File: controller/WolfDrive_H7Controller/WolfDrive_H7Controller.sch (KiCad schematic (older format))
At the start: 320 parts, among them CN10 CONN_02X17, CN7 CONN_02X10, CN8 CONN_02X08, CN9 CONN_02X15, CON1 SD_Card, J1 USB_OTG, J10 GND, J11 GND, J12 12VA, J13 Regen, J14 Throttle, J15 PWM1, J16 PWM2, J17 PWM3, J18 ~PWM1, J19 ~PWM2, J2 QSPI_CLK, J20 ~PWM3, J21 OCV, J22 ~F_C, J23 ~F_B, J24 ~F_A, J25 Overtemp, J26 PWM_EN, J27 Conn_01x04_Female, J28 GS3, J29 Conn_01x04, J3 QSPI_NCS, J30 SPI2_SCK, J31 SPI2_NSS, J32 SPI2_MOSI, J33 SPI2_MISO, J34 PS-DIS, J35 3V3, J36 GND, J37 GND, J38 AGND, J39 SP1_MISO, J4 QSPI_IO0, J40 SP1_SCK, J41 SP1_NSS, J42 SP1_MOSI, J43 GS3, J44 GS3, J45 GS3, J46 GS3, J47 GS3, J48 GS3, J49 GS3, J5 QSPI_IO1, J50 GS3, J51 GS3, J52 GS3, J53 GS3, J54 GS3, J55 GS3, J56 GS3, J6 QSPI_IO2, J7 QSPI_IO3, J8 12V, J9 GND, P1 GATE_IO_A, P10 GATE_IO_A, P11 GATE_IO_A, P7 CONN_01X02, P9 GATE_IO_A, U1 LM1117-5.0, U10 74HC266, U11 FT232RL, U12 74LVC1G02, U13 74LVC1G02, U14 74LVC1G02, U15 74LVC1G02, U16 74LVC1G02, U17 74LVC1G02, U18 74LVC1G02, U19 74LVC1G02, U2 LM1117-3.3, U20 74HC266, U21 74LVC1G02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

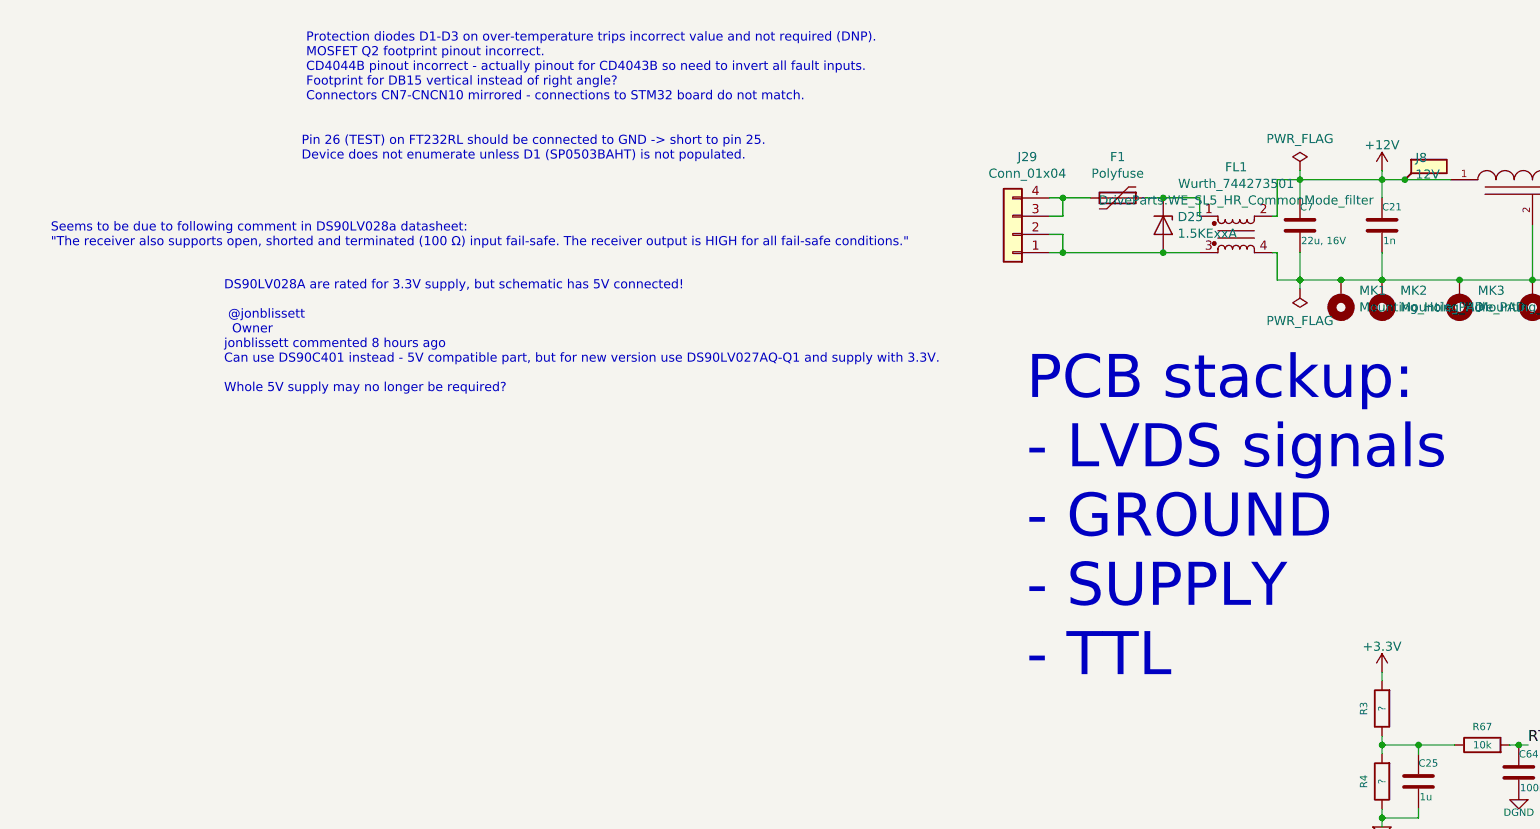
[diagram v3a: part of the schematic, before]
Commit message: Amended input protection
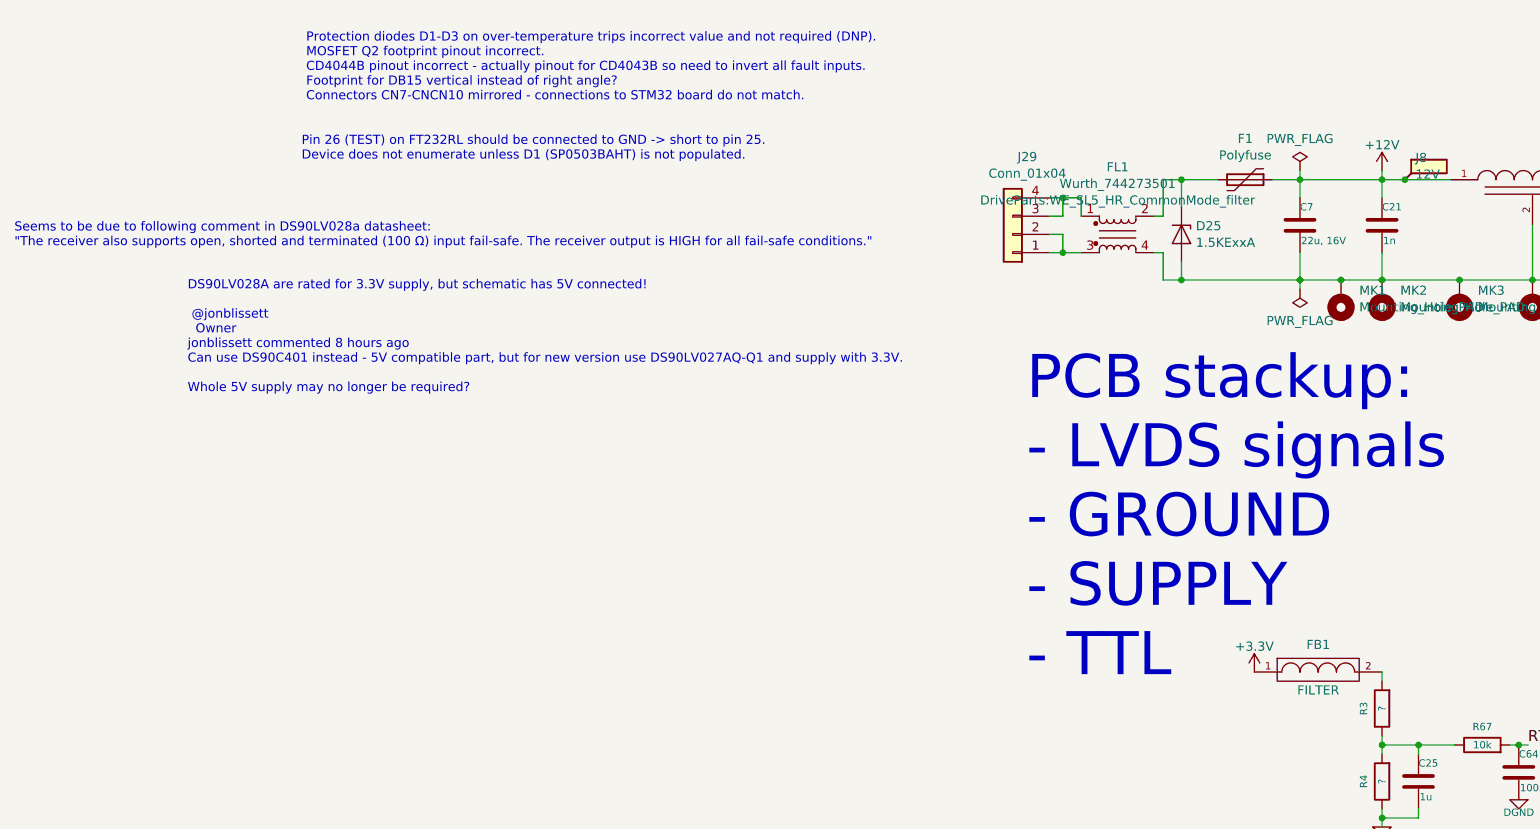
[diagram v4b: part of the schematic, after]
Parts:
- added FB1: FILTER, w_smd_inductors:inductor_smd_0805, symbol WolfDrive_H7Controller-rescue:WolfDrive_H7Controller-rescue_FILTER-RESCUE-WolfD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
- F1: footprint (none) -> Fuse:Fuse_1812_4532Metric_Pad1.24x3.50mm_HandSolder
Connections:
- net +12V: now also F1.1; no longer FL1.2
- net +3V3: now also FB1.1; no longer R3.2
- net DGND: now also D25.2 (A2)
- net at FL1.3, J29.1 (Pin_1), J29.2 (Pin_2): no longer D25.2 (A2)
- net at J29.3 (Pin_3), J29.4 (Pin_4): now also FL1.1; no longer F1.2
- new net: FB1.2, R3.2
- new net: D25.1 (A1), F1.2, FL1.2
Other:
- moved on the sheet: D25, FL1
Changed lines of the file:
@@
 Connection ~ 2450 1550
 Wire Wire Line
-	2325 1550 2450 1550
-Wire Wire Line
 	1075 1850 1150 1850
 Wire Wire Line
@@
 	4275 2000 4275 2100
 Wire Wire Line
-	2325 2100 2450 2100
-Wire Wire Line
 	6150 2625 6350 2625
 Wire Wire Line
@@
 	-1   0    0    1
 $EndComp
-Wire Wire Line
-	1075 1950 1150 1950
-Wire Wire Line
-	1150 1850 1150 1950
 Text Notes 21575 2400 0    50   ~ 0
 SHB11-PBPC-D08-ST-BK
@@
 L Device:EMI_Filter_CommonMode FL1
 U 1 1 5AE9439E
-P 2100 1850
-F 0 "FL1" H 2100 2219 50  0000 C CNN
-F 1 "Wurth_744273501" H 2100 2128 50  0000 C CNN
-F 2 "DriveParts:WE_SL5_HR_CommonMode_filter" H 2100 2037 50  0000 C CNN
-F 3 "~" V 2100 1890 50  0000 C CNN
-	1    2100 1850
+P 1450 1850
+F 0 "FL1" H 1450 2219 50  0000 C CNN
+F 1 "Wurth_744273501" H 1450 2128 50  0000 C CNN
+F 2 "DriveParts:WE_SL5_HR_CommonMode_filter" H 1450 2037 50  0000 C CNN
+F 3 "~" V 1450 1890 50  0000 C CNN
+	1    1450 1850
 	1    0    0    -1
 $EndComp
-Wire Wire Line
-	2325 1550 2325 1750
-Wire Wire Line
-	2325 1750 2300 1750
-Wire Wire Line
-	2300 1950 2325 1950
-Wire Wire Line
-	2325 1950 2325 2100
 Connection ~ 2450 2100
-Connection ~ 1150 1950
 Wire Wire Line
 	1075 1750 1150 1750
@@
 Wire Wire Line
 	9950 4800 10550 4800
-Text Notes -3000 1125 0    50   ~ 0
-Protection diodes D1-D3 on over-temperature trips incorrect value and not required (DNP).\nMOSFET Q2 footprint pinout incorrect.\nCD4044B pinout incorrect - actually pinout for CD4043B so need to invert all fault inputs.\nFootprint for DB15 vertical instead of right angle?\nConnectors CN7-CNCN10 mirrored - connections to STM32 board do not match.
-Text Notes -3025 1450 0    50   ~ 0
-Pin 26 (TEST) on FT232RL should be connected to GND -> short to pin 25.\nDevice does not enumerate unless D1 (SP0503BAHT) is not populated.
-Text Notes -4400 1925 0    50   ~ 0
-Seems to be due to following comment in DS90LV028a datasheet:\n"The receiver also supports open, shorted and terminated (100 Ω) input fail-safe. The receiver output is HIGH for all fail-safe conditions."
-Text Notes -3450 2725 0    50   ~ 0
-DS90LV028A are rated for 3.3V supply, but schematic has 5V connected!\n\n @jonblissett\n  Owner\njonblissett commented 8 hours ago\nCan use DS90C401 instead - 5V compatible part, but for new version use DS90LV027AQ-Q1 and supply with 3.3V.\n\nWhole 5V supply may no longer be required?
 $Comp
 L WolfDrive_H7Controller-rescue:power_+3.3V-RESCUE-WolfDrive_H7Controller-WolfDrive_H7Controller-rescue #PWR0107
@@
 Wire Wire Line
 	21350 12250 21500 12250
-$Comp
-L WolfDrive_H7Controller-rescue:power_+3.3V-RESCUE-WolfDrive_H7Controller-WolfDrive_H7Controller-rescue #PWR0191
-U 1 1 61BC542C
-P 2900 4250
-F 0 "#PWR0191" H 2900 4100 50  0001 C CNN
-F 1 "+3.3V" H 2900 4390 50  0000 C CNN
-F 2 "" H 2900 4250 60  0000 C CNN
-F 3 "" H 2900 4250 60  0000 C CNN
-	1    2900 4250
-	1    0    0    -1
-$EndComp
 Connection ~ 6750 2625
 Wire Wire Line
@@
 	1    0    0    -1
 $EndComp
+Text Notes -3025 1450 0    50   ~ 0
+Pin 26 (TEST) on FT232RL should be connected to GND -> short to pin 25.\nDevice does not enumerate unless D1 (SP0503BAHT) is not populated.
+Text Notes -4600 1925 0    50   ~ 0
+Seems to be due to following comment in DS90LV028a datasheet:\n"The receiver also supports open, shorted and terminated (100 Ω) input fail-safe. The receiver output is HIGH for all fail-safe conditions."
+Text Notes -3000 1125 0    50   ~ 0
+Protection diodes D1-D3 on over-temperature trips incorrect value and not required (DNP).\nMOSFET Q2 footprint pinout incorrect.\nCD4044B pinout incorrect - actually pinout for CD4043B so need to invert all fault inputs.\nFootprint for DB15 vertical instead of right angle?\nConnectors CN7-CNCN10 mirrored - connections to STM32 board do not match.
+Text Notes -3650 2725 0    50   ~ 0
+DS90LV028A are rated for 3.3V supply, but schematic has 5V connected!\n\n @jonblissett\n  Owner\njonblissett commented 8 hours ago\nCan use DS90C401 instead - 5V compatible part, but for new version use DS90LV027AQ-Q1 and supply with 3.3V.\n\nWhole 5V supply may no longer be required?
+Wire Wire Line
+	1150 1850 1150 1950
+Connection ~ 1150 1950
 Wire Wire Line
-	1900 1750 1900 1650
+	1075 1950 1150 1950
+Wire Wire Line
+	1250 1750 1250 1650
+Connection ~ 1150 1650
 $Comp
 L Diode:1.5KExxA D25
 U 1 1 5B0319FA
-P 1700 1800
-F 0 "D25" V 1654 1879 50  0000 L CNN
-F 1 "1.5KExxA" V 1745 1879 50  0000 L CNN
-F 2 "Diode_SMD:D_SMB-SMC_Universal_Handsoldering" H 1700 1600 50  0001 C CNN
-F 3 "https://www.vishay.com/docs/88301/15ke.pdf" H 1650 1800 50  0001 C CNN
-	1    1700 1800
+P 1800 1850
+F 0 "D25" V 1754 1929 50  0000 L CNN
+F 1 "1.5KExxA" V 1845 1929 50  0000 L CNN
+F 2 "Diode_SMD:D_SMB-SMC_Universal_Handsoldering" H 1800 1650 50  0001 C CNN
+F 3 "https://www.vishay.com/docs/88301/15ke.pdf" H 1750 1850 50  0001 C CNN
+	1    1800 1850
 	0    1    1    0
 $EndComp
 Wire Wire Line
-	1150 1950 1700 1950
+	1150 1950 1250 1950
 Wire Wire Line
-	1700 1650 1900 1650
-Connection ~ 1700 1950
-Wire Wire Line
-	1700 1950 1900 1950
+	1150 1650 1250 1650
 $Comp
 L Device:Polyfuse F1
-U 1 1 5B3954F5
-P 1450 1650
-F 0 "F1" V 1225 1650 50  0000 C CNN
-F 1 "Polyfuse" V 1316 1650 50  0000 C CNN
-F 2 "" H 1500 1450 50  0001 L CNN
-F 3 "~" H 1450 1650 50  0001 C CNN
-	1    1450 1650
+U 1 1 5D0A55F3
+P 2150 1550
+F 0 "F1" V 1925 1550 50  0000 C CNN
+F 1 "Polyfuse" V 2016 1550 50  0000 C CNN
+F 2 "Fuse:Fuse_1812_4532Metric_Pad1.24x3.50mm_HandSolder" H 2200 1350 50  0001 L CNN
+F 3 "~" H 2150 1550 50  0001 C CNN
+	1    2150 1550
 	0    1    1    0
 $EndComp
 Wire Wire Line
-	1300 1650 1150 1650
-Connection ~ 1150 1650
+	2300 1550 2450 1550
+Wire Wire Line
+	2000 1550 1800 1550
+Wire Wire Line
+	1800 1550 1800 1700
+Wire Wire Line
+	1650 1750 1700 1750
+Wire Wire Line
+	1700 1750 1700 1550
 Wire Wire Line
-	1600 1650 1700 1650
-Connection ~ 1700 1650
+	1700 1550 1800 1550
+Connection ~ 1800 1550
+Wire Wire Line
+	1650 1950 1700 1950
+Wire Wire Line
+	1700 1950 1700 2100
+Wire Wire Line
+	1700 2100 1800 2100
+Wire Wire Line
+	1800 2000 1800 2100
+Connection ~ 1800 2100
+Wire Wire Line
+	1800 2100 2450 2100
+$Comp
+L WolfDrive_H7Controller-rescue:power_+3.3V-RESCUE-WolfDrive_H7Controller-WolfDrive_H7Controller-rescue #PWR0191
+U 1 1 61BC542C
+P 2200 4250
+F 0 "#PWR0191" H 2200 4100 50  0001 C CNN
+F 1 "+3.3V" H 2200 4390 50  0000 C CNN
+F 2 "" H 2200 4250 60  0000 C CNN
+F 3 "" H 2200 4250 60  0000 C CNN
+	1    2200 4250
+	1    0    0    -1
+$EndComp
+$Comp
+L WolfDrive_H7Controller-rescue:WolfDrive_H7Controller-rescue_FILTER-RESCUE-WolfDrive_H7Controller-WolfDrive_H7Controller-rescue FB1
+U 1 1 5D76AC8F
+P 2550 4250
+F 0 "FB1" H 2550 4400 50  0000 C CNN
+F 1 "FILTER" H 2550 4150 50  0000 C CNN
+F 2 "w_smd_inductors:inductor_smd_0805" H 2550 4250 50  0001 C CNN
+F 3 "" H 2550 4250 50  0000 C CNN
+	1    2550 4250
+	1    0    0    -1
+$EndComp
 $EndSCHEMATC

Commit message: updated footprints
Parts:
- P1, P10, P11, P9: footprint Connectors:IDC_Header_Straight_16pins -> Connectors_IDC:IDC-Header_2x08_Pitch2.54mm_Straight
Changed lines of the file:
@@
 F 0 "P10" H 21625 4225 50  0000 C CNN
 F 1 "GATE_IO_A" V 21625 3775 50  0000 C CNN
-F 2 "Connectors:IDC_Header_Straight_16pins" H 21625 2575 50  0001 C CNN
+F 2 "Connectors_IDC:IDC-Header_2x08_Pitch2.54mm_Straight" H 21625 2575 50  0001 C CNN
 F 3 "" H 21625 2575 50  0000 C CNN
 	1    21625 3775
@@
 F 0 "P11" H 21625 6325 50  0000 C CNN
 F 1 "GATE_IO_A" V 21625 5875 50  0000 C CNN
-F 2 "Connectors:IDC_Header_Straight_16pins" H 21625 4675 50  0001 C CNN
+F 2 "Connectors_IDC:IDC-Header_2x08_Pitch2.54mm_Straight" H 21625 4675 50  0001 C CNN
 F 3 "" H 21625 4675 50  0000 C CNN
 	1    21625 5875
@@
 F 0 "P9" H 21625 2275 50  0000 C CNN
 F 1 "GATE_IO_A" V 21625 1825 50  0000 C CNN
-F 2 "Connectors:IDC_Header_Straight_16pins" H 21625 625 50  0001 C CNN
+F 2 "Connectors_IDC:IDC-Header_2x08_Pitch2.54mm_Straight" H 21625 625 50  0001 C CNN
 F 3 "" H 21625 625 50  0000 C CNN
 	1    21625 1825
@@
 F 0 "P1" H 9900 10950 50  0000 C CNN
 F 1 "GATE_IO_A" V 9900 10500 50  0000 C CNN
-F 2 "Connectors:IDC_Header_Straight_16pins" H 9900 9300 50  0001 C CNN
+F 2 "Connectors_IDC:IDC-Header_2x08_Pitch2.54mm_Straight" H 9900 9300 50  0001 C CNN
 F 3 "" H 9900 9300 50  0000 C CNN
 	1    9900 10500

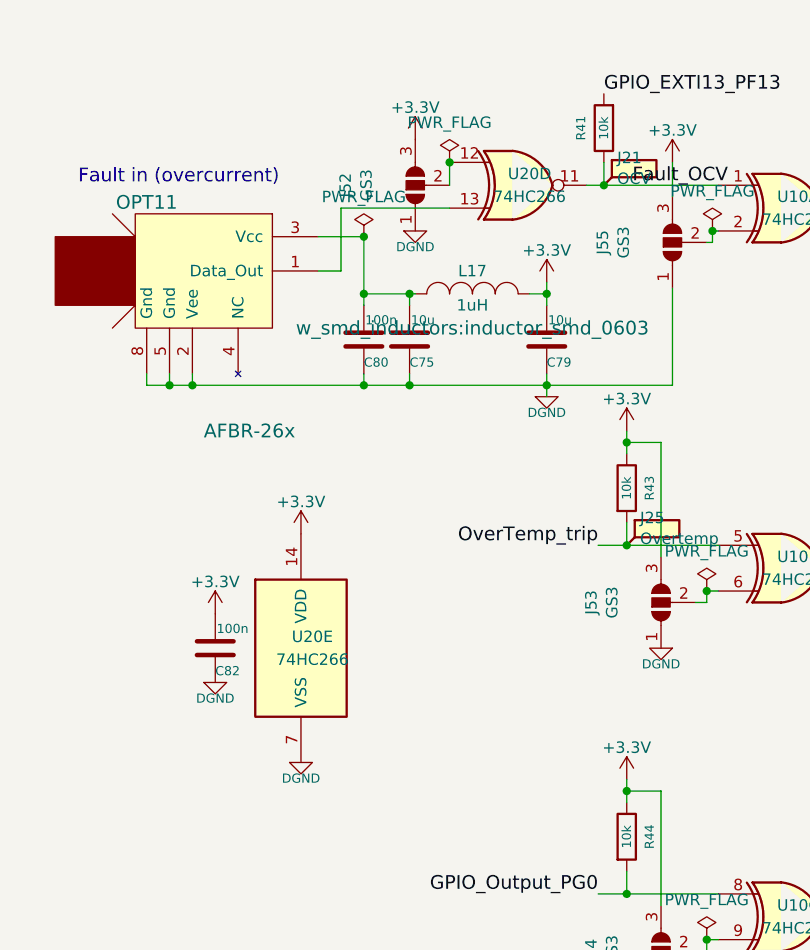
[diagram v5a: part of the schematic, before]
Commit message: fixed duplicate gates in U10
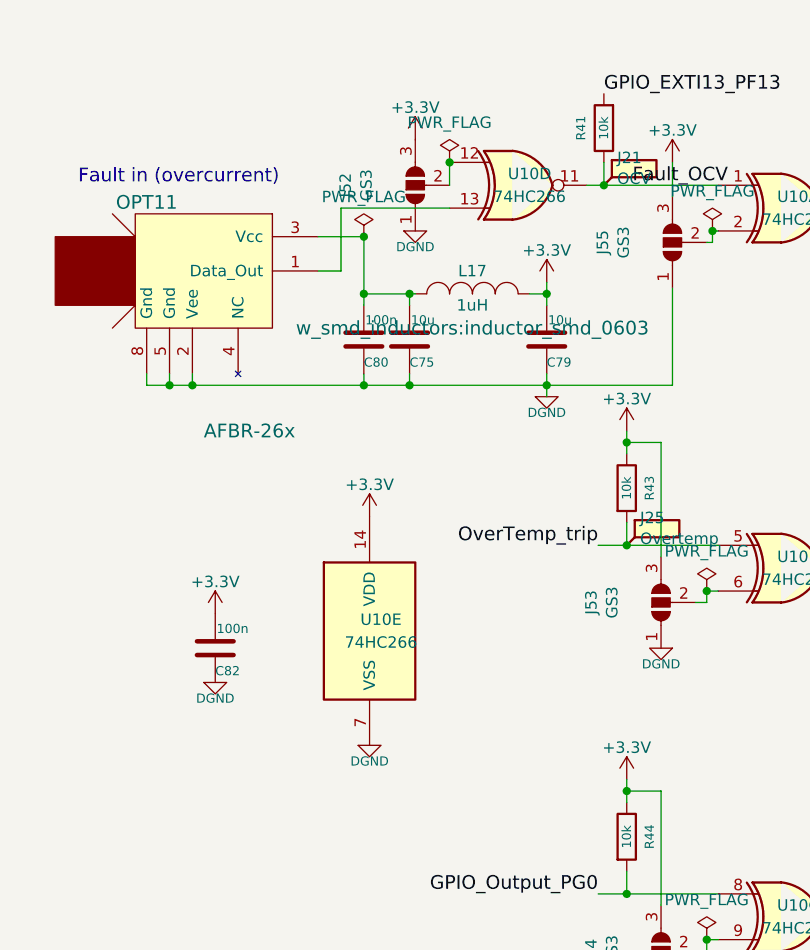
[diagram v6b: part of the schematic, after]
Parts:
- removed U20: 74HC266, Housings_SOIC:SOIC-14_3.9x8.7mm_Pitch1.27mm, symbol 4xxx:4077
- added unit 4 of U10
- added unit 5 of U10
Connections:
- net +3V3: now also U10.14 (VDD)
- net DGND: now also U10.7 (VSS)
- net Fault_OCV: now also U10.11
- net at OPT11.1 (Data_Out): now also U10.13
- net at J52.2 (C): now also U10.12
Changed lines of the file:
@@
 L WolfDrive_H7Controller-rescue:WolfDrive_H7Controller-rescue_DGND-RESCUE-WolfDrive_H7Controller-WolfDrive_H7Controller-rescue #PWR0123
 U 1 1 61BD1640
-P 19100 10475
-F 0 "#PWR0123" H 19100 10475 40  0001 C CNN
-F 1 "DGND" H 19100 10405 40  0000 C CNN
-F 2 "" H 19100 10475 60  0000 C CNN
-F 3 "" H 19100 10475 60  0000 C CNN
-	1    19100 10475
+P 19400 10400
+F 0 "#PWR0123" H 19400 10400 40  0001 C CNN
+F 1 "DGND" H 19400 10330 40  0000 C CNN
+F 2 "" H 19400 10400 60  0000 C CNN
+F 3 "" H 19400 10400 60  0000 C CNN
+	1    19400 10400
 	1    0    0    -1
 $EndComp
@@
 L WolfDrive_H7Controller-rescue:power_+3.3V-RESCUE-WolfDrive_H7Controller-WolfDrive_H7Controller-rescue #PWR0171
 U 1 1 5B06A297
-P 19100 9475
-F 0 "#PWR0171" H 19100 9325 50  0001 C CNN
-F 1 "+3.3V" H 19100 9615 50  0000 C CNN
-F 2 "" H 19100 9475 60  0000 C CNN
-F 3 "" H 19100 9475 60  0000 C CNN
-	1    19100 9475
+P 19400 9400
+F 0 "#PWR0171" H 19400 9250 50  0001 C CNN
+F 1 "+3.3V" H 19400 9540 50  0000 C CNN
+F 2 "" H 19400 9400 60  0000 C CNN
+F 3 "" H 19400 9400 60  0000 C CNN
+	1    19400 9400
 	-1   0    0    -1
 $EndComp
@@
 Wire Wire Line
 	2450 2100 2675 2100
-$Comp
-L 4xxx:4077 U20
-U 5 1 5B2E4377
-P 19100 9975
-F 0 "U20" H 19150 10025 50  0000 C CNN
-F 1 "74HC266" H 19150 9925 50  0000 C CNN
-F 2 "Housings_SOIC:SOIC-14_3.9x8.7mm_Pitch1.27mm" H 19100 9975 50  0001 C CNN
-F 3 "" H 19100 9975 50  0000 C CNN
-	5    19100 9975
-	1    0    0    -1
-$EndComp
 Wire Wire Line
 	900  10275 900  10500
@@
 Connection ~ 21675 9625
 $Comp
-L 4xxx:4077 U20
-U 4 1 5EA8658B
-P 20050 7950
-F 0 "U20" H 20100 8000 50  0000 C CNN
-F 1 "74HC266" H 20100 7900 50  0000 C CNN
-F 2 "Housings_SOIC:SOIC-14_3.9x8.7mm_Pitch1.27mm" H 20050 7950 50  0001 C CNN
-F 3 "" H 20050 7950 50  0000 C CNN
-	4    20050 7950
-	1    0    0    -1
-$EndComp
-$Comp
 L Jumper:SolderJumper_3_Open J55
 U 1 1 5EA89362
@@
 	1    0    0    -1
 $EndComp
-Connection ~ 19750 7850
 $Comp
 L WolfDrive_H7Controller-rescue:power_+3.3V-RESCUE-WolfDrive_H7Controller-WolfDrive_H7Controller-rescue #PWR0175
@@
 	1    0    0    -1
 $EndComp
+$Comp
+L 4xxx:4077 U10
+U 4 1 5AE24BD8
+P 20050 7950
+F 0 "U10" H 20100 8000 50  0000 C CNN
+F 1 "74HC266" H 20100 7900 50  0000 C CNN
+F 2 "Housings_SOIC:SOIC-14_3.9x8.7mm_Pitch1.27mm" H 20050 7950 50  0001 C CNN
+F 3 "" H 20050 7950 50  0000 C CNN
+	4    20050 7950
+	1    0    0    -1
+$EndComp
+Connection ~ 19750 7850
+$Comp
+L 4xxx:4077 U10
+U 5 1 5AE252AC
+P 19400 9900
+F 0 "U10" H 19450 9950 50  0000 C CNN
+F 1 "74HC266" H 19450 9850 50  0000 C CNN
+F 2 "Housings_SOIC:SOIC-14_3.9x8.7mm_Pitch1.27mm" H 19400 9900 50  0001 C CNN
+F 3 "" H 19400 9900 50  0000 C CNN
+	5    19400 9900
+	1    0    0    -1
+$EndComp
